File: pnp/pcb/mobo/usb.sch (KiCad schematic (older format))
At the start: 13 parts, among them J41 USB_B, J42 Conn_01x09_Male, U6 CH340G, U8 FE1.1S, Y2 12MHz, Y3 12MHz

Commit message: updated power sheet to have 3V3 LDO
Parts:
- U8: symbol index:FE1.1S -> mobo-rescue:FE1.1S-index
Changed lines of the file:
@@
 	1700 4100 1700 4000
 $Comp
-L index:FE1.1S U8
+L mobo-rescue:FE1.1S-index U8
 U 1 1 5EEBF8BF
 P 4700 3150

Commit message: got rid of the CH340G, as the STM32 has native USB. separated vbus from main 5v rail to prevent the buck converter from fighting the usb 5V reference
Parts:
- removed C21, C22: 10pF, Capacitor_SMD:C_0805_2012Metric_Pad1.15x1.40mm_HandSolder, symbol Device:C_Small
- removed C23: 10nF, Capacitor_SMD:C_0805_2012Metric_Pad1.15x1.40mm_HandSolder, symbol Device:C_Small
- removed U6: CH340G, Package_SO:SOIC-16_3.9x9.9mm_P1.27mm, symbol Interface_USB:CH340G
- removed Y3: 12MHz, Crystal:Crystal_SMD_HC49-SD, symbol Device:Crystal_GND3
- J42: value Conn_01x09_Male -> Stacked_USBA
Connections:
- net labels added: VBUS
- net labels removed: CTS, DTR, RX, TX
- wire segments 47 -> 26
- no-connect marks 13 -> 8
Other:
- moved on the sheet: C18, C19, C20, J41, J42, R41, U8

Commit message: added spi to motor drivers
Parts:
- Y2: footprint Crystal:Crystal_SMD_HC49-SD -> Crystal:Crystal_SMD_0603-2Pin_6.0x3.5mm
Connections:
- net labels added: uC_D+, uC_D-
- net labels removed: 4D+, 4D-
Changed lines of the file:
@@
 F 0 "Y2" H 2650 1350 50  0000 L CNN
 F 1 "12MHz" H 2600 1650 50  0000 L CNN
-F 2 "Crystal:Crystal_SMD_HC49-SD" H 2700 1500 50  0001 C CNN
+F 2 "Crystal:Crystal_SMD_0603-2Pin_6.0x3.5mm" H 2700 1500 50  0001 C CNN
 F 3 "~" H 2700 1500 50  0001 C CNN
 	1    2700 1500
@@
 Text GLabel 3250 1900 0    50   Input ~ 0
 3D+
-Text GLabel 3250 2000 0    50   Input ~ 0
-4D-
-Text GLabel 3250 2100 0    50   Input ~ 0
-4D+
 $Comp
 L power:GND #PWR0308
@@
 Connection ~ 7150 2050
 $Comp
-L power:VBUS #PWR?
+L power:VBUS #PWR0180
 U 1 1 5F12A579
 P 1550 1150
-F 0 "#PWR?" H 1550 1000 50  0001 C CNN
+F 0 "#PWR0180" H 1550 1000 50  0001 C CNN
 F 1 "VBUS" H 1565 1323 50  0000 C CNN
 F 2 "" H 1550 1150 50  0001 C CNN
@@
 Wire Wire Line
 	6700 1400 6900 1400
+Text GLabel 3250 2100 0    50   Input ~ 0
+uC_D+
+Text GLabel 3250 2000 0    50   Input ~ 0
+uC_D-
 $EndSCHEMATC

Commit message: finished layout, going to try a different one, committing in case i mess it up
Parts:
- removed Y2: 12MHz, Crystal:Crystal_SMD_0603-2Pin_6.0x3.5mm, symbol Device:Crystal
- added Y2: 12MHz, Crystal:Crystal_SMD_3225-4Pin_3.2x2.5mm, symbol Device:Crystal_GND24_Small
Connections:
- wire segments 26 -> 33
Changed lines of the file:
@@
-$EndComp
-$Comp
-L Device:Crystal Y2
-U 1 1 5EEC262D
-P 2700 1500
-F 0 "Y2" H 2650 1350 50  0000 L CNN
-F 1 "12MHz" H 2600 1650 50  0000 L CNN
-F 2 "Crystal:Crystal_SMD_0603-2Pin_6.0x3.5mm" H 2700 1500 50  0001 C CNN
-F 3 "~" H 2700 1500 50  0001 C CNN
-	1    2700 1500
-	-1   0    0    1
 $EndComp
 $Comp
@@
 Text GLabel 3250 2000 0    50   Input ~ 0
 uC_D-
+$Comp
+L Device:Crystal_GND24_Small Y?
+U 1 1 5F21A5A5
+P 2700 1500
+AR Path="/5F21A5A5" Ref="Y?"  Part="1"
+AR Path="/5EB0C6B9/5F21A5A5" Ref="Y2"  Part="1"
+F 0 "Y2" H 2844 1546 50  0000 L CNN
+F 1 "12MHz" H 2550 1650 50  0000 L CNN
+F 2 "Crystal:Crystal_SMD_3225-4Pin_3.2x2.5mm" H 2700 1500 50  0001 C CNN
+F 3 "~" H 2700 1500 50  0001 C CNN
+	1    2700 1500
+	1    0    0    -1
+$EndComp
+Wire Wire Line
+	2550 1500 2600 1500
+Wire Wire Line
+	2800 1500 2850 1500
+$Comp
+L power:GND #PWR0147
+U 1 1 5F21B287
+P 2700 1725
+F 0 "#PWR0147" H 2700 1475 50  0001 C CNN
+F 1 "GND" H 2600 1725 50  0000 C CNN
+F 2 "" H 2700 1725 50  0001 C CNN
+F 3 "" H 2700 1725 50  0001 C CNN
+	1    2700 1725
+	1    0    0    -1
+$EndComp
+Wire Wire Line
+	2700 1725 2700 1675
+Wire Wire Line
+	2700 1375 2825 1375
+Wire Wire Line
+	2825 1375 2825 1675
+Wire Wire Line
+	2825 1675 2700 1675
+Connection ~ 2700 1675
+Wire Wire Line
+	2700 1675 2700 1625
 $EndSCHEMATC

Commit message: a few other files tweaked in the routing process
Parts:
- Y2: symbol Device:Crystal_GND24_Small -> mobo-rescue:Crystal_GND24_Small-Device
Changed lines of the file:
@@
 uC_D-
 $Comp
-L Device:Crystal_GND24_Small Y?
+L mobo-rescue:Crystal_GND24_Small-Device Y?
 U 1 1 5F21A5A5
 P 2700 1500

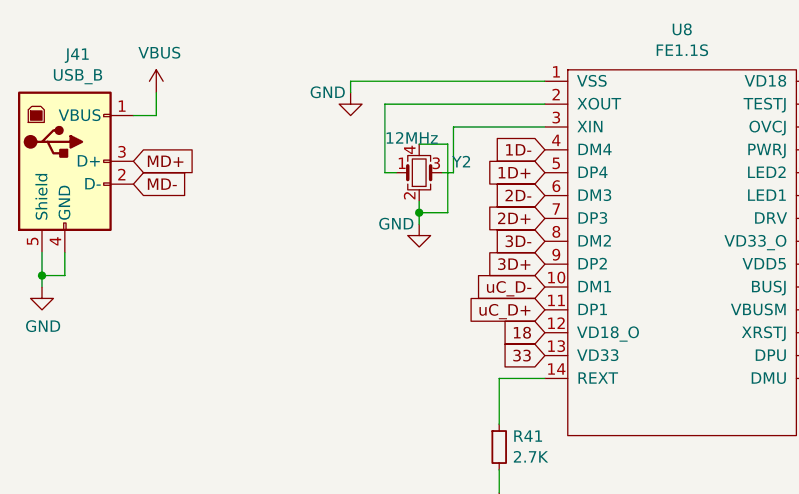
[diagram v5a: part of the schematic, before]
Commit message: added 12v routing to increase current allowed
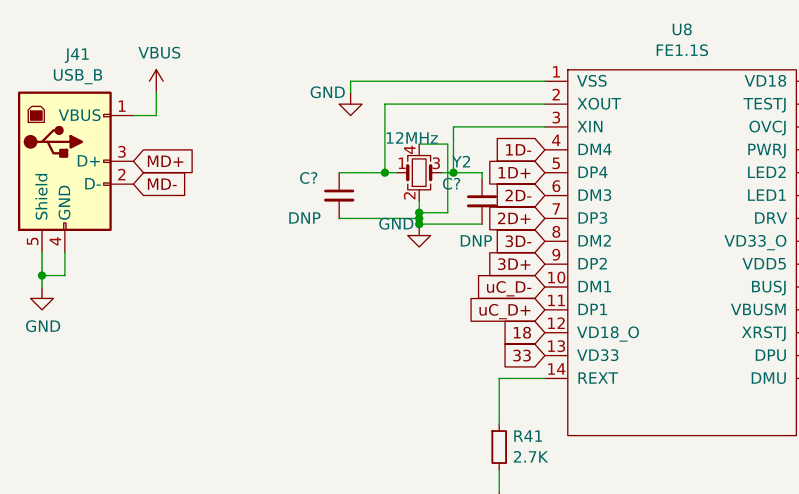
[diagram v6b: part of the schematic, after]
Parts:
- added C? (x2): DNP, Capacitor_SMD:C_0805_2012Metric_Pad1.15x1.40mm_HandSolder, symbol Device:C_Small
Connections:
- net GND: now also C?.2, C?.2
- net at U8.2 (XOUT), Y2.1: now also C?.1
- net at U8.3 (XIN), Y2.3: now also C?.1
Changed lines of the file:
@@
 $EndComp
 Wire Wire Line
-	2700 1725 2700 1675
+	2700 1725 2700 1700
 Wire Wire Line
 	2700 1375 2825 1375
@@
 Wire Wire Line
 	2700 1675 2700 1625
+$Comp
+L Device:C_Small C?
+U 1 1 5FA60D00
+P 2350 1600
+F 0 "C?" H 2175 1675 50  0000 L CNN
+F 1 "DNP" H 2125 1500 50  0000 L CNN
+F 2 "Capacitor_SMD:C_0805_2012Metric_Pad1.15x1.40mm_HandSolder" H 2350 1600 50  0001 C CNN
+F 3 "~" H 2350 1600 50  0001 C CNN
+	1    2350 1600
+	1    0    0    -1
+$EndComp
+Wire Wire Line
+	2350 1500 2550 1500
+Connection ~ 2550 1500
+Wire Wire Line
+	2350 1700 2700 1700
+Wire Wire Line
+	2700 1700 2700 1675
+Connection ~ 2700 1700
+$Comp
+L Device:C_Small C?
+U 1 1 5FA62D6B
+P 2975 1625
+F 0 "C?" H 2800 1700 50  0000 L CNN
+F 1 "DNP" H 2875 1450 50  0000 L CNN
+F 2 "Capacitor_SMD:C_0805_2012Metric_Pad1.15x1.40mm_HandSolder" H 2975 1625 50  0001 C CNN
+F 3 "~" H 2975 1625 50  0001 C CNN
+	1    2975 1625
+	1    0    0    -1
+$EndComp
+Wire Wire Line
+	2850 1500 2975 1500
+Wire Wire Line
+	2975 1500 2975 1525
+Connection ~ 2850 1500
+Wire Wire Line
+	2975 1725 2700 1725
+Connection ~ 2700 1725
 $EndSCHEMATC

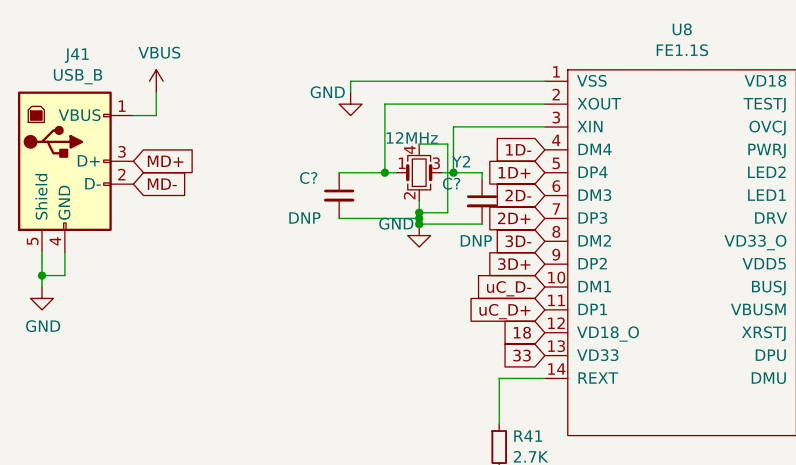
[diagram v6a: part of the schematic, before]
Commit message: usb routing mostly redone
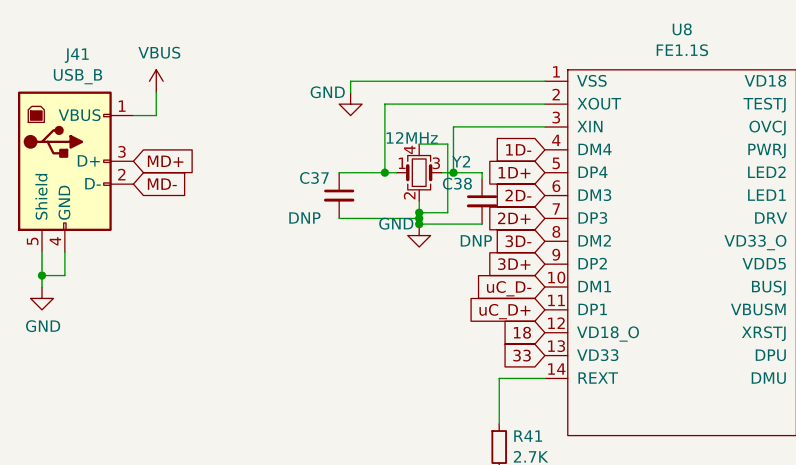
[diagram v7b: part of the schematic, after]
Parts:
- gave numbers to parts that had none: 2
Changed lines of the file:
@@
 	2700 1675 2700 1625
 $Comp
-L Device:C_Small C?
+L Device:C_Small C37
 U 1 1 5FA60D00
 P 2350 1600
-F 0 "C?" H 2175 1675 50  0000 L CNN
+F 0 "C37" H 2175 1675 50  0000 L CNN
 F 1 "DNP" H 2125 1500 50  0000 L CNN
 F 2 "Capacitor_SMD:C_0805_2012Metric_Pad1.15x1.40mm_HandSolder" H 2350 1600 50  0001 C CNN
@@
 Connection ~ 2700 1700
 $Comp
-L Device:C_Small C?
+L Device:C_Small C38
 U 1 1 5FA62D6B
 P 2975 1625
-F 0 "C?" H 2800 1700 50  0000 L CNN
+F 0 "C38" H 2800 1700 50  0000 L CNN
 F 1 "DNP" H 2875 1450 50  0000 L CNN
 F 2 "Capacitor_SMD:C_0805_2012Metric_Pad1.15x1.40mm_HandSolder" H 2975 1625 50  0001 C CNN

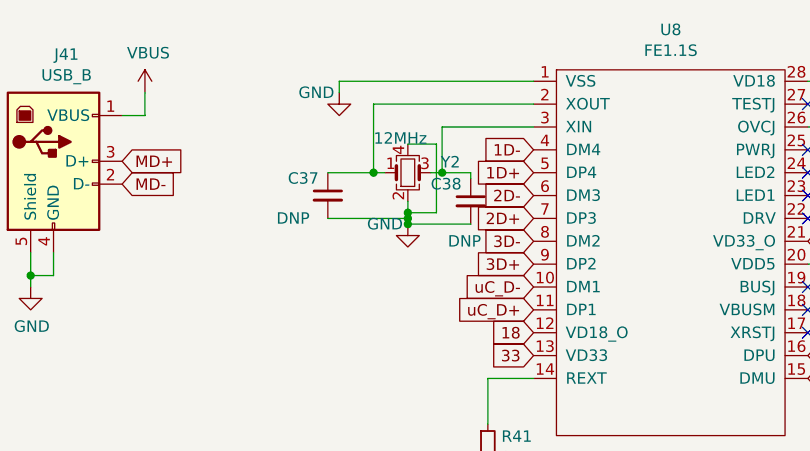
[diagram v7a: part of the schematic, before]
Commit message: clean up USB crystal schematic
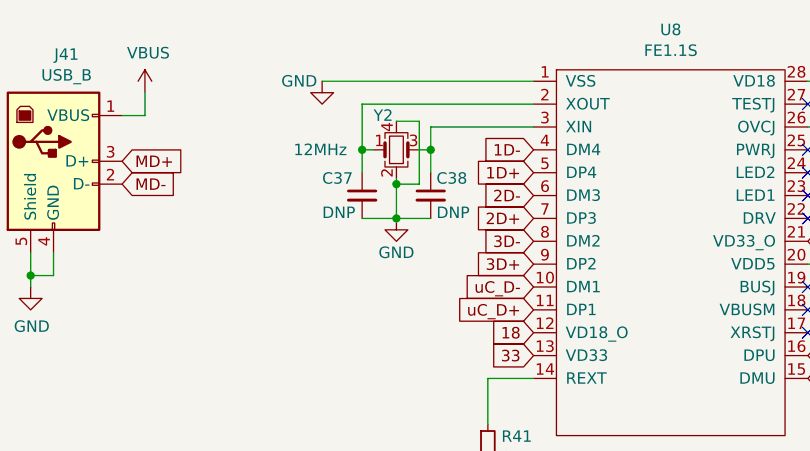
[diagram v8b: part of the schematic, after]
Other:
- moved on the sheet: C37, C38, Y2
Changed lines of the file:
@@
 L power:GND #PWR0307
 U 1 1 5EEC28DF
-P 2400 1150
-F 0 "#PWR0307" H 2400 900 50  0001 C CNN
-F 1 "GND" H 2300 1150 50  0000 C CNN
-F 2 "" H 2400 1150 50  0001 C CNN
-F 3 "" H 2400 1150 50  0001 C CNN
-	1    2400 1150
-	1    0    0    -1
-$EndComp
-Wire Wire Line
-	2400 1150 2400 1100
-Wire Wire Line
-	2850 1500 2850 1300
-Wire Wire Line
-	2850 1300 3250 1300
-Wire Wire Line
-	3250 1200 2550 1200
-Wire Wire Line
-	2550 1200 2550 1500
+P 2325 1100
+F 0 "#PWR0307" H 2325 850 50  0001 C CNN
+F 1 "GND" H 2225 1100 50  0000 C CNN
+F 2 "" H 2325 1100 50  0001 C CNN
+F 3 "" H 2325 1100 50  0001 C CNN
+	1    2325 1100
+	1    0    0    -1
+$EndComp
 Text GLabel 3250 1400 0    50   Input ~ 0
 1D-
@@
 $EndComp
 Wire Wire Line
-	2400 1100 3250 1100
-Wire Wire Line
 	6700 1450 6700 1400
 Wire Wire Line
@@
 uC_D-
 $Comp
+L power:GND #PWR0147
+U 1 1 5F21B287
+P 2650 1700
+F 0 "#PWR0147" H 2650 1450 50  0001 C CNN
+F 1 "GND" H 2650 1550 50  0000 C CNN
+F 2 "" H 2650 1700 50  0001 C CNN
+F 3 "" H 2650 1700 50  0001 C CNN
+	1    2650 1700
+	1    0    0    -1
+$EndComp
+$Comp
+L Device:C_Small C37
+U 1 1 5FA60D00
+P 2500 1600
+F 0 "C37" H 2325 1675 50  0000 L CNN
+F 1 "DNP" H 2325 1525 50  0000 L CNN
+F 2 "Capacitor_SMD:C_0805_2012Metric_Pad1.15x1.40mm_HandSolder" H 2500 1600 50  0001 C CNN
+F 3 "~" H 2500 1600 50  0001 C CNN
+	1    2500 1600
+	1    0    0    -1
+$EndComp
+$Comp
+L Device:C_Small C38
+U 1 1 5FA62D6B
+P 2800 1600
+F 0 "C38" H 2825 1675 50  0000 L CNN
+F 1 "DNP" H 2825 1525 50  0000 L CNN
+F 2 "Capacitor_SMD:C_0805_2012Metric_Pad1.15x1.40mm_HandSolder" H 2800 1600 50  0001 C CNN
+F 3 "~" H 2800 1600 50  0001 C CNN
+	1    2800 1600
+	1    0    0    -1
+$EndComp
+$Comp
 L mobo-rescue:Crystal_GND24_Small-Device Y?
 U 1 1 5F21A5A5
-P 2700 1500
+P 2650 1400
 AR Path="/5F21A5A5" Ref="Y?"  Part="1"
 AR Path="/5EB0C6B9/5F21A5A5" Ref="Y2"  Part="1"
-F 0 "Y2" H 2844 1546 50  0000 L CNN
-F 1 "12MHz" H 2550 1650 50  0000 L CNN
-F 2 "Crystal:Crystal_SMD_3225-4Pin_3.2x2.5mm" H 2700 1500 50  0001 C CNN
-F 3 "~" H 2700 1500 50  0001 C CNN
-	1    2700 1500
-	1    0    0    -1
-$EndComp
-Wire Wire Line
-	2550 1500 2600 1500
-Wire Wire Line
-	2800 1500 2850 1500
-$Comp
-L power:GND #PWR0147
-U 1 1 5F21B287
-P 2700 1725
-F 0 "#PWR0147" H 2700 1475 50  0001 C CNN
-F 1 "GND" H 2600 1725 50  0000 C CNN
-F 2 "" H 2700 1725 50  0001 C CNN
-F 3 "" H 2700 1725 50  0001 C CNN
-	1    2700 1725
-	1    0    0    -1
-$EndComp
-Wire Wire Line
-	2700 1725 2700 1700
-Wire Wire Line
-	2700 1375 2825 1375
-Wire Wire Line
-	2825 1375 2825 1675
-Wire Wire Line
-	2825 1675 2700 1675
-Connection ~ 2700 1675
-Wire Wire Line
-	2700 1675 2700 1625
-$Comp
-L Device:C_Small C37
-U 1 1 5FA60D00
-P 2350 1600
-F 0 "C37" H 2175 1675 50  0000 L CNN
-F 1 "DNP" H 2125 1500 50  0000 L CNN
-F 2 "Capacitor_SMD:C_0805_2012Metric_Pad1.15x1.40mm_HandSolder" H 2350 1600 50  0001 C CNN
-F 3 "~" H 2350 1600 50  0001 C CNN
-	1    2350 1600
-	1    0    0    -1
-$EndComp
-Wire Wire Line
-	2350 1500 2550 1500
-Connection ~ 2550 1500
-Wire Wire Line
-	2350 1700 2700 1700
-Wire Wire Line
-	2700 1700 2700 1675
-Connection ~ 2700 1700
-$Comp
-L Device:C_Small C38
-U 1 1 5FA62D6B
-P 2975 1625
-F 0 "C38" H 2800 1700 50  0000 L CNN
-F 1 "DNP" H 2875 1450 50  0000 L CNN
-F 2 "Capacitor_SMD:C_0805_2012Metric_Pad1.15x1.40mm_HandSolder" H 2975 1625 50  0001 C CNN
-F 3 "~" H 2975 1625 50  0001 C CNN
-	1    2975 1625
-	1    0    0    -1
-$EndComp
-Wire Wire Line
-	2850 1500 2975 1500
-Wire Wire Line
-	2975 1500 2975 1525
-Connection ~ 2850 1500
-Wire Wire Line
-	2975 1725 2700 1725
-Connection ~ 2700 1725
+F 0 "Y2" H 2550 1550 50  0000 L CNN
+F 1 "12MHz" H 2200 1400 50  0000 L CNN
+F 2 "Crystal:Crystal_SMD_3225-4Pin_3.2x2.5mm" H 2650 1400 50  0001 C CNN
+F 3 "~" H 2650 1400 50  0001 C CNN
+	1    2650 1400
+	1    0    0    -1
+$EndComp
+Wire Wire Line
+	2750 1400 2800 1400
+Wire Wire Line
+	2800 1400 2800 1500
+Wire Wire Line
+	2550 1400 2500 1400
+Wire Wire Line
+	2500 1400 2500 1500
+Wire Wire Line
+	2500 1700 2650 1700
+Wire Wire Line
+	2650 1525 2650 1550
+Connection ~ 2650 1700
+Wire Wire Line
+	2800 1700 2650 1700
+Wire Wire Line
+	2650 1275 2750 1275
+Wire Wire Line
+	2750 1550 2650 1550
+Connection ~ 2650 1550
+Wire Wire Line
+	2650 1550 2650 1700
+Wire Wire Line
+	2800 1300 2800 1400
+Wire Wire Line
+	2800 1300 3250 1300
+Connection ~ 2800 1400
+Wire Wire Line
+	2500 1200 2500 1400
+Wire Wire Line
+	2500 1200 3250 1200
+Connection ~ 2500 1400
+Wire Wire Line
+	2325 1100 3250 1100
+Wire Wire Line
+	2750 1275 2750 1550
 $EndSCHEMATC
